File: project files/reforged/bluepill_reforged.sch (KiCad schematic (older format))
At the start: 41 parts, among them J1 USB_C_Receptacle_USB2.0, J2 Left Castellation, J3 Right Castellation, J4 STDC14-THT, J5 STDC14-SMD, SW1 Boot0, SW2 Reset, U1 STM32F103C8Tx, U2 AMS1117-3.3, Y1 MC-306, 32768Hz, Y2 8MHz

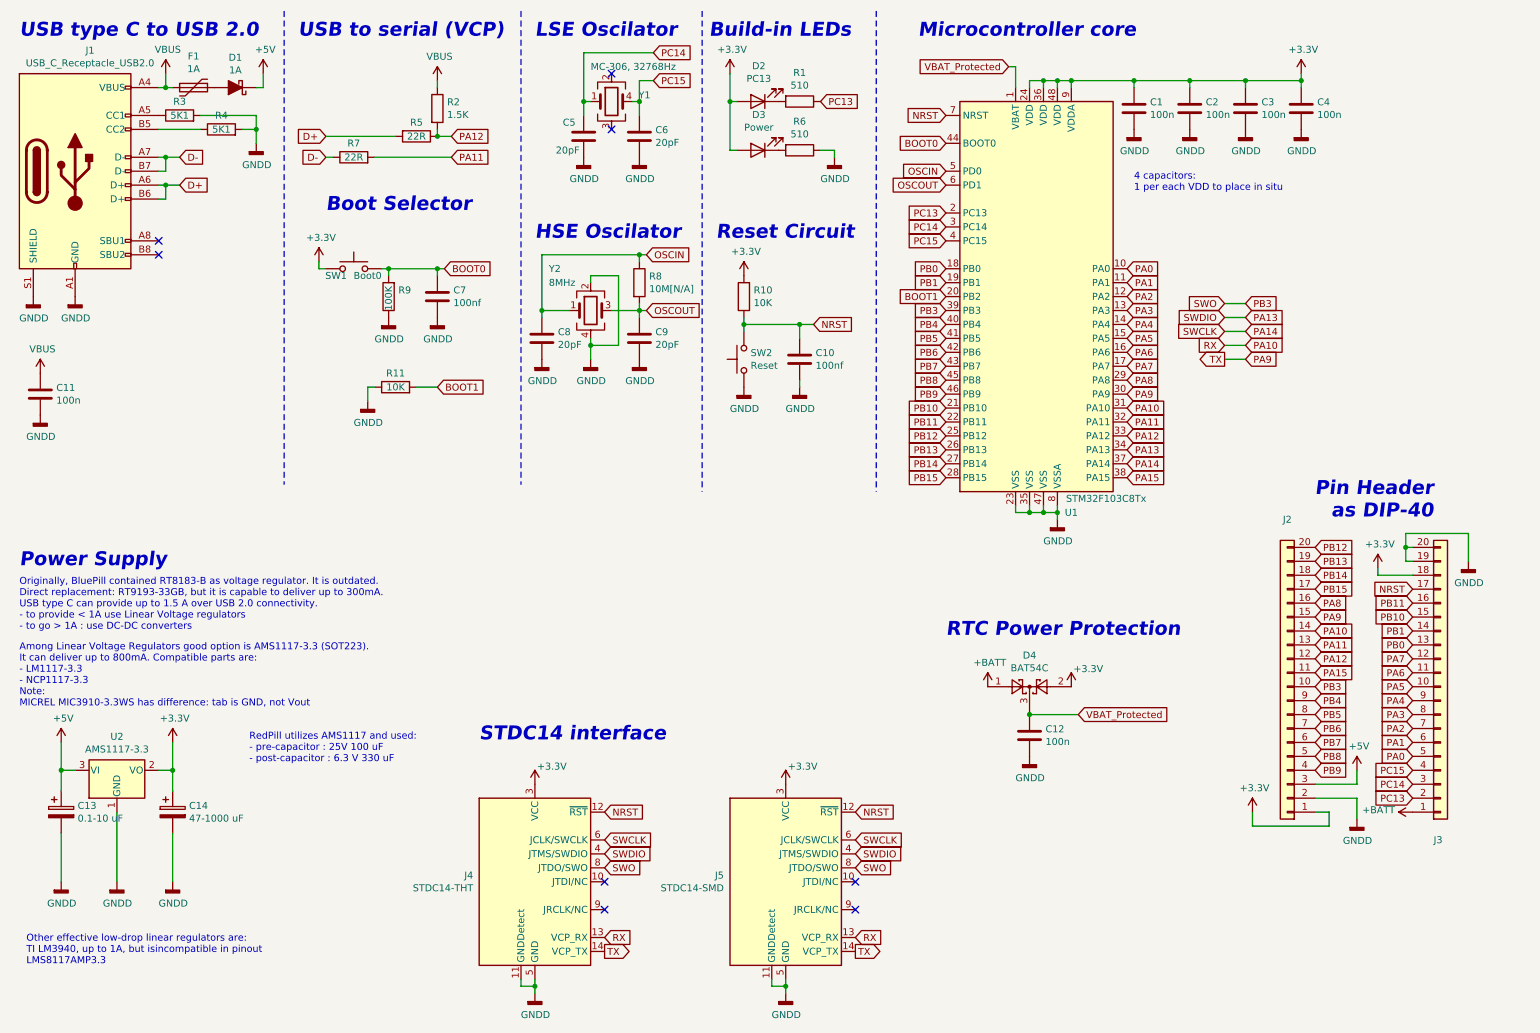
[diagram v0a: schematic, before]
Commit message: Added lo-pass filter for VCCA
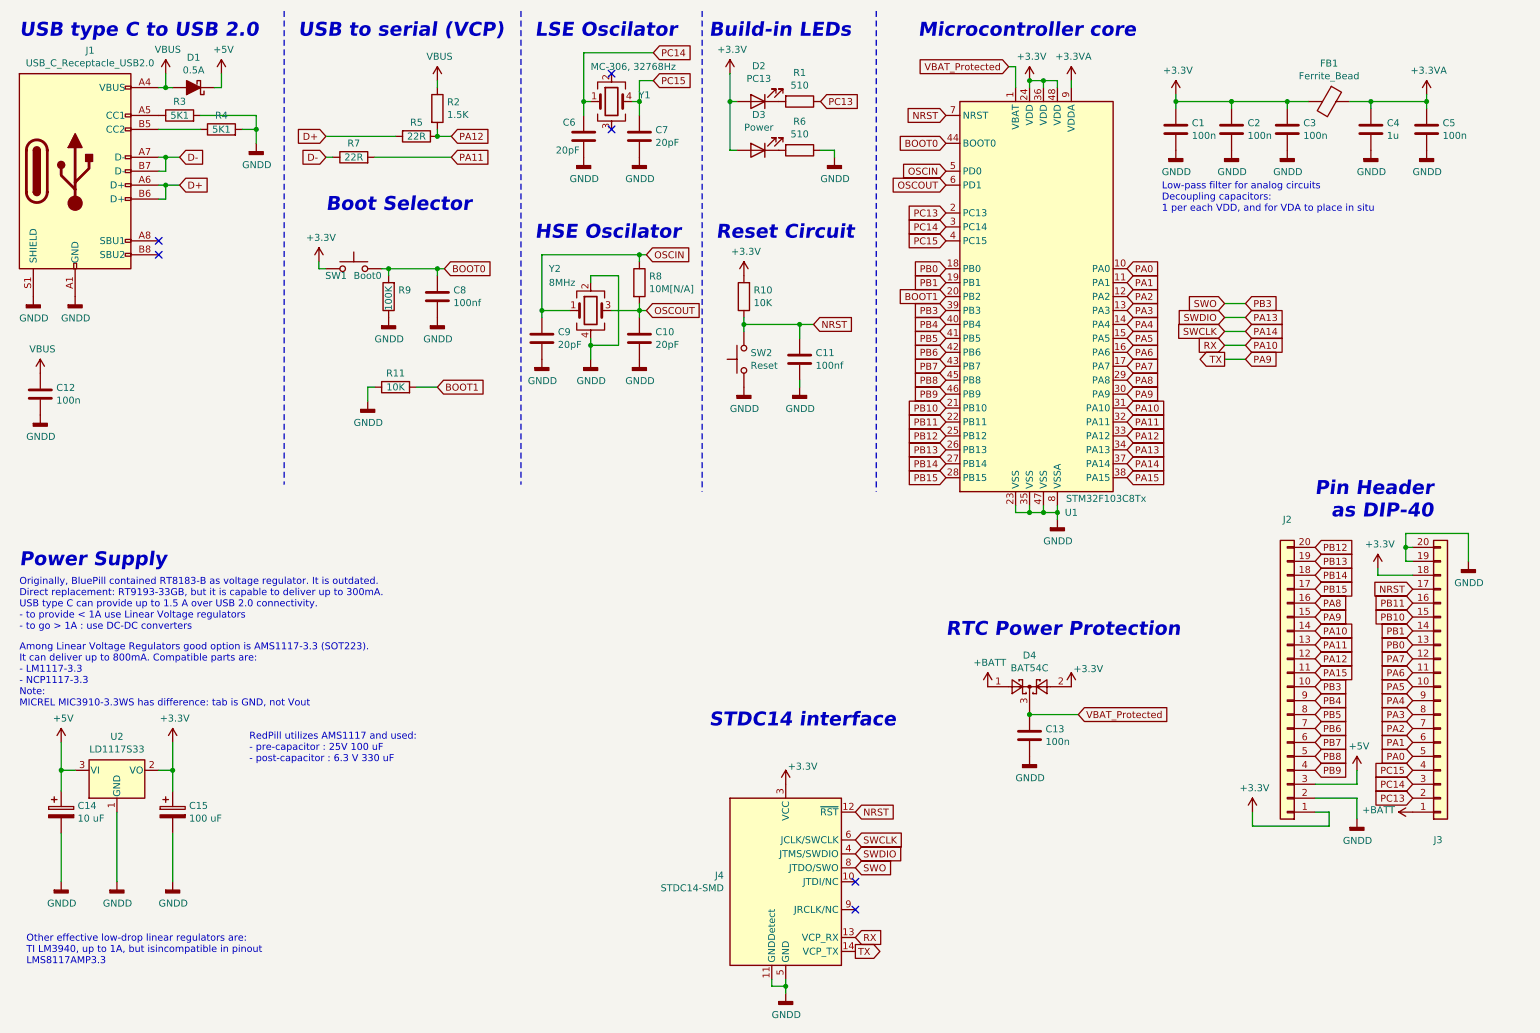
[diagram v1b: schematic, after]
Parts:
- removed F1: 1A, Fuse:Fuse_0805_2012Metric, symbol Device:Polyfuse
- removed J4: STDC14-THT, Connector_PinHeader_1.27mm:PinHeader_2x07_P1.27mm_Vertical, symbol Connector:Conn_ST_STDC14
- removed U2: AMS1117-3.3, Package_TO_SOT_SMD:SOT-223-3_TabPin2, symbol Regulator_Linear:AMS1117-3.3
- added C4: 1u, Capacitor_SMD:C_0603_1608Metric_Pad1.05x0.95mm_HandSolder, symbol Device:C
- added FB1: Ferrite_Bead, Inductor_SMD:L_0805_2012Metric, symbol Device:Ferrite_Bead
- added U2: LD1117S33, Package_TO_SOT_SMD:SOT-223-3_TabPin2, symbol Regulator_Linear:LD1117S33TR_SOT223
- C14: renamed from C13; value 0.1-10 uF -> 10 uF
- C15: renamed from C14; value 47-1000 uF -> 100 uF
- D1: value 1A -> 0.5A
- renumbered C9 to C10, C10 to C11, C11 to C12, C12 to C13, C4 to C5, C5 to C6, C6 to C7, C7 to C8, C8 to C9, J5 to J4
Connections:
- net +3V3: now also FB1.2, U2.2 (VO); no longer C5.1, U1.9 (VDDA)
- net +5V: now also U2.3 (VI)
- net GNDD: now also C4.2, U2.1 (GND)
- net VBUS: now also D1.2 (A)
- new net +3.3VA: C4.1, C5.1, FB1.1, U1.9 (VDDA)
- no-connect marks 8 -> 6
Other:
- note added: "Low-pass filter for analog circuits\nDecoupling capacitors: \n1 per each VDD, and for VDA to place in situ"
- note removed: "4 capacitors: \n1 per each VDD to place in situ"
- moved on the sheet: C1, C2, C3, C5, D1

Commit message: Update bluepill_reforged.sch
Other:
- note added: "On some boards top pin\non this header is +5V after diode"
- note added: "On some boards, USER LED\nis attached from PB2 to GND"
- note added: "Pin Headers as DIP-40"
- note removed: "Pin Header\nas DIP-40"
- moved on the sheet: C13, C14, C15, D4, J2, J3, J4, U2

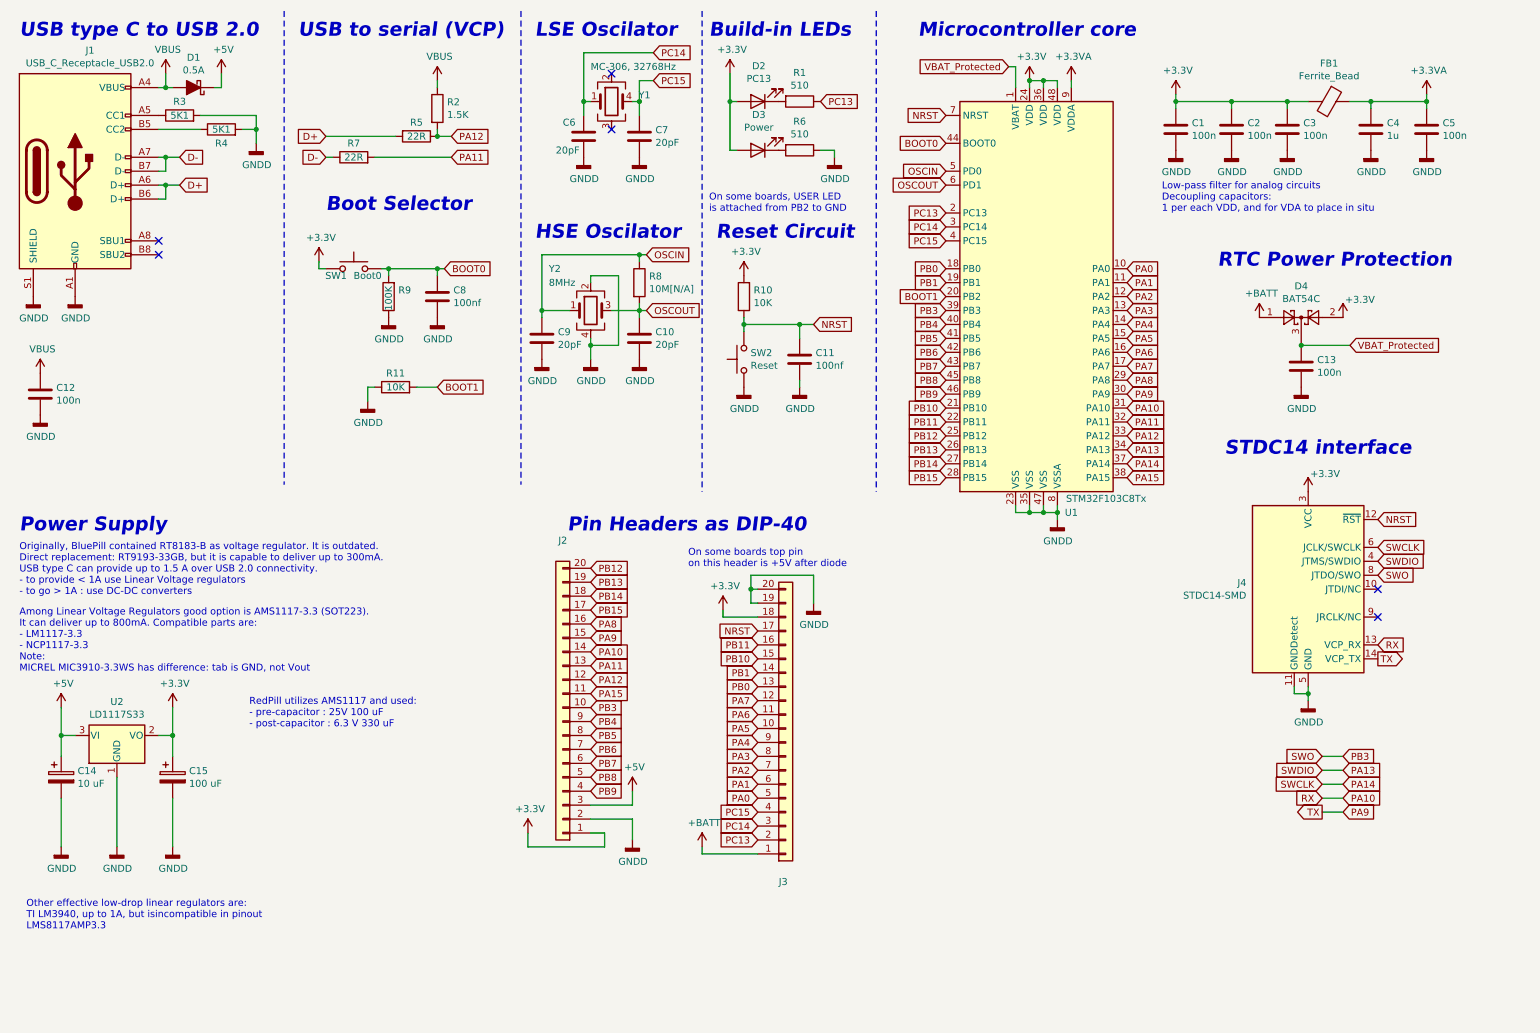
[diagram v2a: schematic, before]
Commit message: Added QWIIC connector
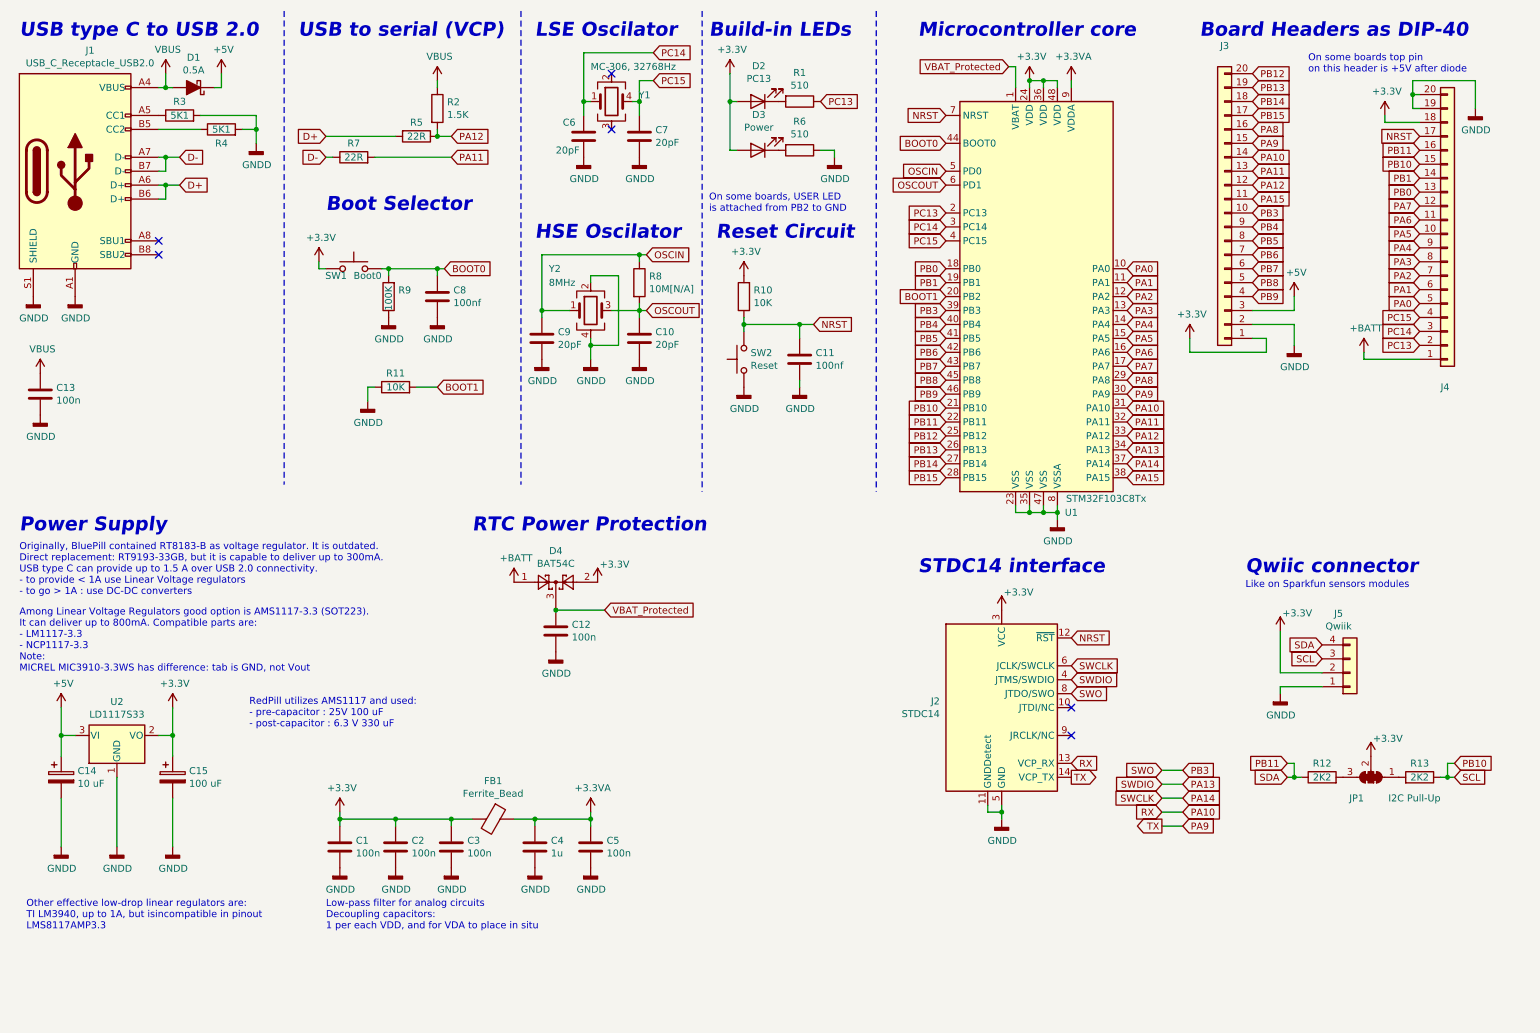
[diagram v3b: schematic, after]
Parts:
- added J5: Qwiik, Connector_JST:JST_SH_SM04B-SRSS-TB_1x04-1MP_P1.00mm_Horizontal, symbol Connector_Generic:Conn_01x04
- added JP1: I2C Pull-Up, Jumper:SolderJumper-3_P2.0mm_Open_TrianglePad1.0x1.5mm_NumberLabels, symbol Jumper:SolderJumper_3_Bridged123
- added R12, R13: 2K2, Resistor_SMD:R_0603_1608Metric_Pad1.05x0.95mm_HandSolder, symbol Device:R
- J2: renamed from J4; value STDC14-SMD -> STDC14
- renumbered C13 to C12, C12 to C13, J2 to J3, J3 to J4
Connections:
- net +3V3: now also J5.2 (Pin_2), JP1.2 (C)
- net GNDD: now also J5.1 (Pin_1)
- net PB10: now also J5.3 (Pin_3), R13.1
- net PB11: now also J5.4 (Pin_4), R12.1
- new net: JP1.3 (B), R12.2
- new net: JP1.1 (A), R13.2
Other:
- note added: "Board Headers as DIP-40"
- note added: "Like on Sparkfun sensors modules"
- note added: "Qwiic connector"
- note removed: "Pin Headers as DIP-40"
- moved on the sheet: C1, C12, C2, C3, C4, C5, D4, FB1, J2, J3, J4
